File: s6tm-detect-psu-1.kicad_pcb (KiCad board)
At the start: 4 copper layers, 115 parts, among them J1 Conn_01x02, J2 Conn_01x02, J3 USB_C_Receptacle_USB2.0_14P, J4 Conn_01x04, J5 Conn_01x04, J6 Conn_01x04_Pin, J7 TC2030, SW1 SW_Push, SW2 SW_Push, U1 TPS259470x, U2 TPS259470x, U3 TPS259470x, U4 TPS62933, U5 TPS259470x, U6 SN65HVD230, U7 HT753-1, U8 STM32F103C8Tx, Y1 8M

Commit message: pcb: initial sectionning
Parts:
- moved D11 271.3 mm to (268.1, 71.2), turned to 90 degrees
- moved Y1 256.8 mm to (268.3, 61.2), turned to 90 degrees
- moved R27 254.0 mm to (271.9, 66.8), turned to 90 degrees
- moved D15 252.6 mm to (263.8, 34.9)
- moved C37 251.0 mm to (261.2, 39.2)
- moved SW1 250.8 mm to (247.0, 66.2)
- moved SW2 250.8 mm to (247.0, 70.8)
- moved C30 250.6 mm to (269.4, 66.8), turned to 90 degrees
- moved C29 247.2 mm to (266.9, 66.8), turned to 90 degrees
- moved J6 247.1 mm to (256.6, 71.1), turned to 90 degrees
- moved R28 246.0 mm to (272.6, 72.0), turned to 90 degrees
- moved U7 246.0 mm to (263.2, 92.3)
- moved R26 243.5 mm to (270.6, 72.0), turned to 90 degrees
- moved C27 240.9 mm to (272.4, 58.1), turned to 90 degrees
- moved C36 237.5 mm to (267.1, 74.9), turned to 90 degrees
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
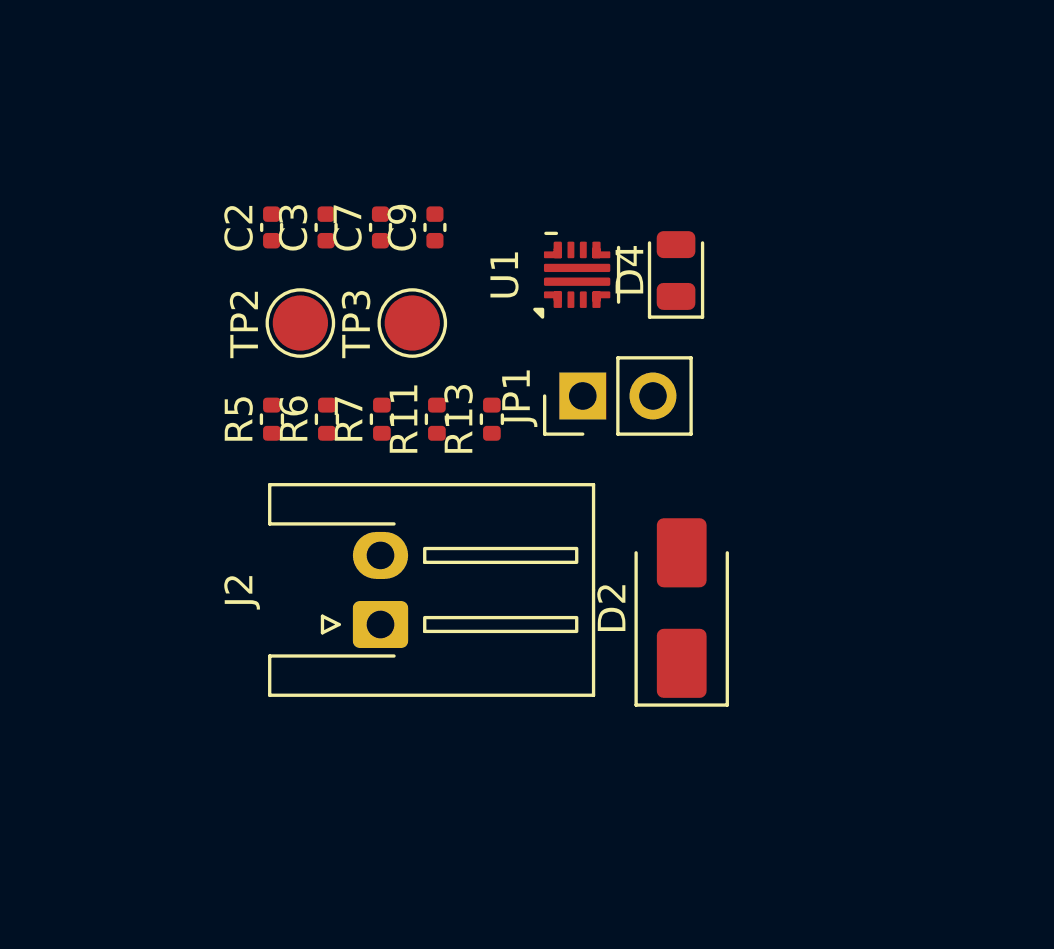
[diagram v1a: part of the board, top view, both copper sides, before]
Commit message: schem: update some 10u footprints
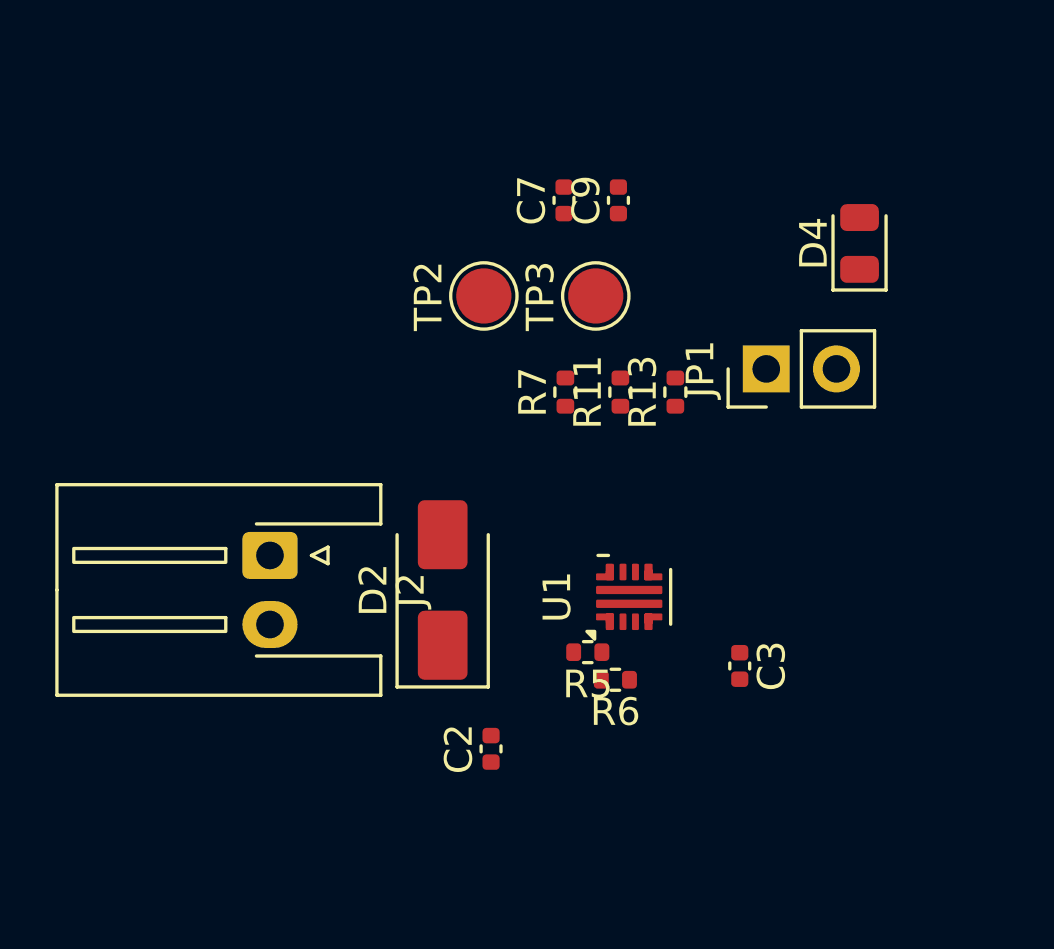
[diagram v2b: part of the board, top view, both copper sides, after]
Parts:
- moved C3 21.8 mm to (113.5, 61.0), turned to -90 degrees
- moved C2 20.5 mm to (104.5, 64.0)
- moved R5 14.2 mm to (108.0, 60.5), turned to 180 degrees
- moved R6 14.1 mm to (109.0, 61.5), turned to 180 degrees
- moved U1 11.8 mm to (109.5, 58.5)
- moved D2 8.67 mm to (102.8, 58.2)
- moved C7 6.71 mm to (107.1, 44.1)
- moved C9 6.71 mm to (109.1, 44.1)
- moved TP2 6.71 mm to (104.2, 47.6)
- moved TP3 6.71 mm to (108.3, 47.6)
- moved D4 6.71 mm to (117.8, 45.7)
- moved JP1 6.71 mm to (114.5, 50.2)
- moved R11 6.71 mm to (109.2, 51.1)
- moved R13 6.71 mm to (111.2, 51.1)
- moved R7 6.71 mm to (107.2, 51.1)
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
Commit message: pcb: add efuse 1 layout
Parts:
- C10, C7, C8, C9: footprint Capacitor_SMD:C_0402_1005Metric -> Capacitor_SMD:C_0805_2012Metric
- moved D4 17.0 mm to (110.5, 61.0), turned to 0 degrees
- moved C9 15.0 mm to (111.5, 59.0), turned to 0 degrees
- moved C7 12.6 mm to (110.8, 56.2)
- moved R13 12.3 mm to (107.3, 62.8), turned to 0 degrees
- moved R11 10.5 mm to (112.8, 61.0)
- moved C3 6.73 mm to (109.0, 56.0), turned to 90 degrees
- moved R7 5.42 mm to (107.5, 56.5), turned to 180 degrees
- moved C2 3.25 mm to (105.8, 61.0)
- moved R6 1.77 mm to (107.2, 61.8)
- moved U1 1.25 mm to (108.2, 58.5)
- moved R5 0.79 mm to (107.2, 60.8)

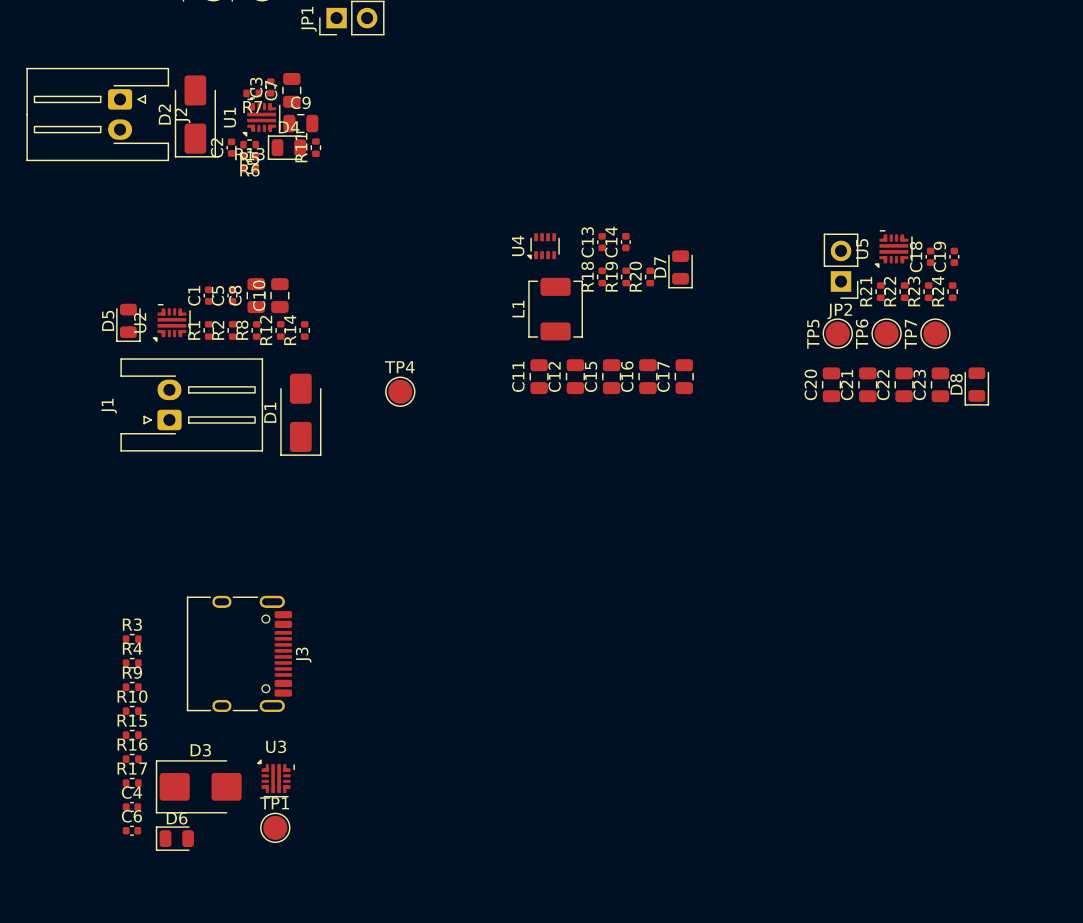
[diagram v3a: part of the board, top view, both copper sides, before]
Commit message: pcb: add efuse routing
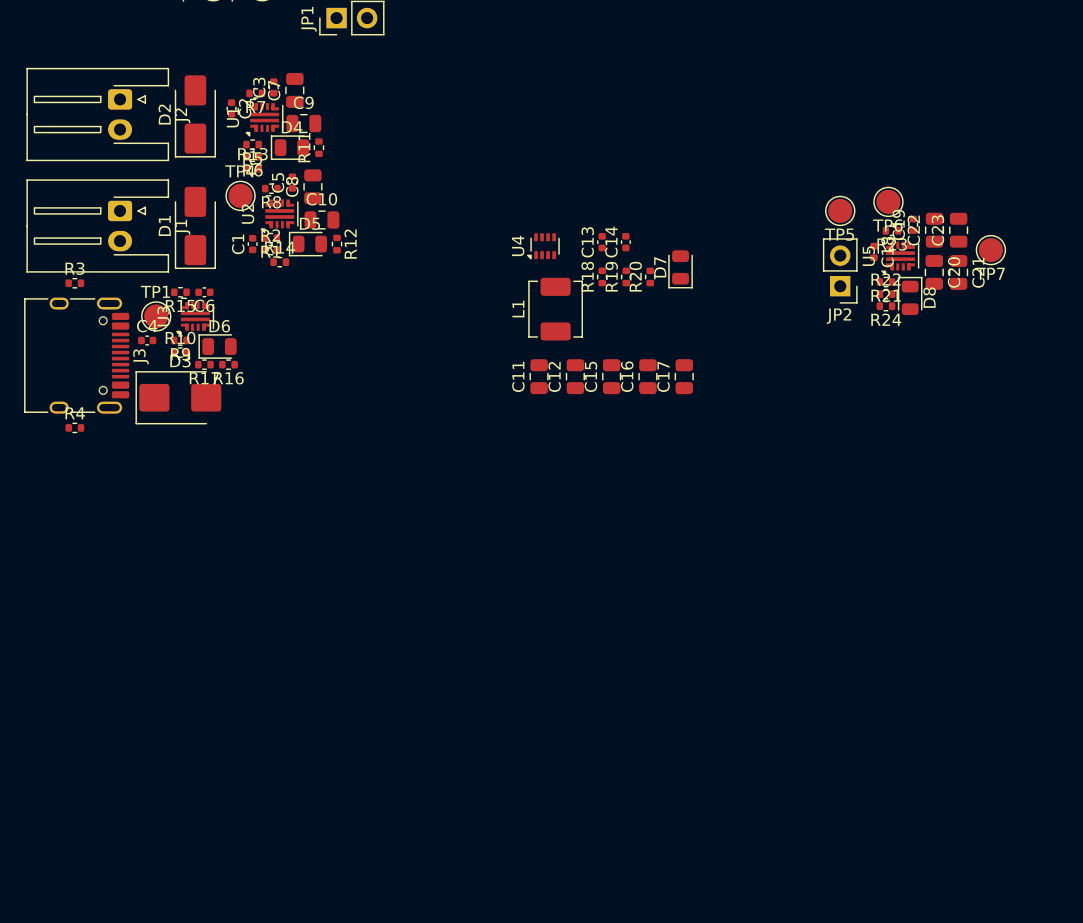
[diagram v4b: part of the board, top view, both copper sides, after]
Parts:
- moved C6 45.1 mm to (103.5, 73.0), turned to 180 degrees
- moved TP1 43.6 mm to (99.5, 75.0)
- moved D6 41.0 mm to (104.8, 77.5)
- moved U3 38.9 mm to (102.8, 75.0), turned to 90 degrees
- moved C4 38.7 mm to (98.8, 77.0)
- moved R15 37.0 mm to (101.5, 73.0), turned to 180 degrees
- moved R17 35.2 mm to (103.5, 79.0), turned to 180 degrees
- moved R16 33.7 mm to (105.5, 79.0), turned to 180 degrees
- moved D3 32.3 mm to (101.5, 81.8)
- moved R10 30.0 mm to (101.5, 78.0)
- moved R3 29.9 mm to (92.8, 72.2)
- moved R9 29.0 mm to (101.5, 77.0), turned to 180 degrees
- moved J3 28.2 mm to (92.5, 78.2)
- moved TP4 21.0 mm to (106.5, 65.0)
- moved R4 20.1 mm to (92.8, 84.2)
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
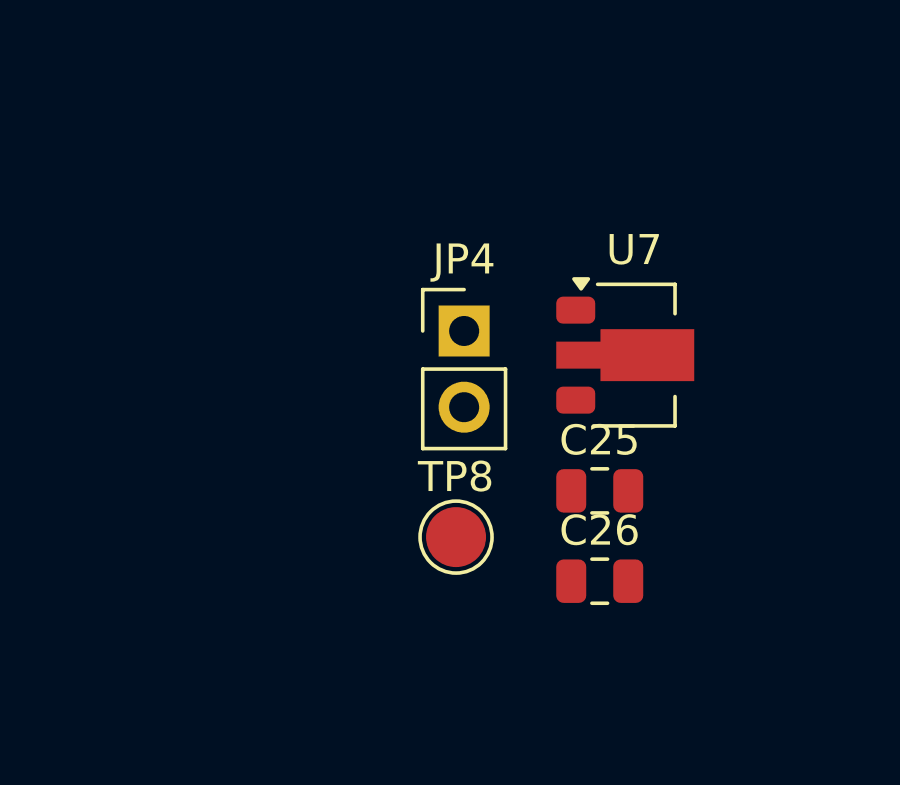
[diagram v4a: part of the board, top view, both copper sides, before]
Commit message: pcb: add ldo layout
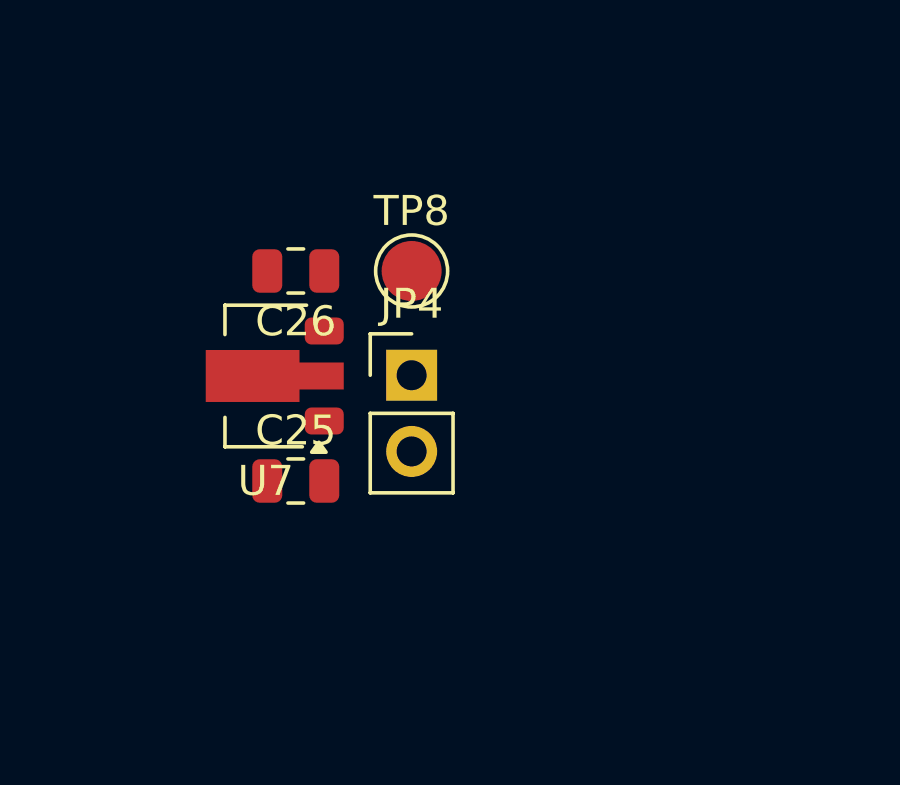
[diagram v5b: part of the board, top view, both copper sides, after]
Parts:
- moved C26 14.5 mm to (251.9, 89.5), turned to 180 degrees
- moved U7 12.3 mm to (250.9, 93.0), turned to 180 degrees
- moved C25 10.1 mm to (251.9, 96.5)
- moved TP8 8.99 mm to (255.8, 89.5)
- moved JP4 2.29 mm to (255.8, 93.0)
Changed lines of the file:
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@@
 	(footprint "TestPoint:TestPoint_Pad_D2.0mm"
 		(layer "F.Cu")
-		(at 257.23 98.37)
+		(at 255.75 89.5)
 		(descr "SMD pad as test Point, diameter 2.0mm")
 		(tags "test point SMD pad")
@@
 	(footprint "Capacitor_SMD:C_0805_2012Metric"
 		(layer "F.Cu")
-		(at 262.02 99.84)
+		(at 251.8875 89.5 180)
 		(descr "Capacitor SMD 0805 (2012 Metric), square (rectangular) end terminal, IPC-7351 nominal, (Body size source: IPC-SM-782 page 76, https://www.pcb-3d.com/wordpress/wp-content/uploads/ipc-sm-782a_amendment_1_and_2.pdf, https://docs.google.com/spreadsheets/d/1BsfQQcO9C6DZCsRaXUlFlo91Tg2WpOkGARC1WS5S8t0/edit?usp=sharing)")
 		(tags "capacitor")
@@
 		)
 		(property "Basic" "Y"
-			(at 0 0 0)
+			(at 0 0 180)
 			(unlocked yes)
 			(layer "F.Fab")
@@
 		)
 		(property "JLCPCB Part #" "C440198"
-			(at 0 0 0)
+			(at 0 0 180)
 			(unlocked yes)
 			(layer "F.Fab")
@@
 		)
 		(property "Manufacturer" "Murata"
-			(at 0 0 0)
+			(at 0 0 180)
 			(unlocked yes)
 			(layer "F.Fab")
@@
 		)
 		(property "Manufacturer Part Number" "GRM21BR61H106KE43L"
-			(at 0 0 0)
+			(at 0 0 180)
 			(unlocked yes)
 			(layer "F.Fab")
@@
 		(duplicate_pad_numbers_are_jumpers no)
 		(fp_line
-			(start -0.261252 -0.735)
-			(end 0.261252 -0.735)
+			(start -0.261252 0.735)
+			(end 0.261252 0.735)
 			(stroke
 				(width 0.12)
@@
 		)
 		(fp_line
-			(start -0.261252 0.735)
-			(end 0.261252 0.735)
+			(start -0.261252 -0.735)
+			(end 0.261252 -0.735)
 			(stroke
 				(width 0.12)
@@
 		)
 		(pad "1" smd roundrect
-			(at -0.95 0)
+			(at -0.95 0 180)
 			(size 1 1.45)
 			(layers "F.Cu" "F.Mask" "F.Paste")
@@
 		)
 		(pad "2" smd roundrect
-			(at 0.95 0)
+			(at 0.95 0 180)
 			(size 1 1.45)
 			(layers "F.Cu" "F.Mask" "F.Paste")
@@
 	(footprint "Capacitor_SMD:C_0805_2012Metric"
 		(layer "F.Cu")
-		(at 262.02 96.83)
+		(at 251.8875 96.5)
 		(descr "Capacitor SMD 0805 (2012 Metric), square (rectangular) end terminal, IPC-7351 nominal, (Body size source: IPC-SM-782 page 76, https://www.pcb-3d.com/wordpress/wp-content/uploads/ipc-sm-782a_amendment_1_and_2.pdf, https://docs.google.com/spreadsheets/d/1BsfQQcO9C6DZCsRaXUlFlo91Tg2WpOkGARC1WS5S8t0/edit?usp=sharing)")
 		(tags "capacitor")
@@
 	(footprint "Connector_PinHeader_2.54mm:PinHeader_1x02_P2.54mm_Vertical"
 		(layer "F.Cu")
-		(at 257.5 91.5)
+		(at 255.75 92.975)
 		(descr "Through hole straight pin header, 1x02, 2.54mm pitch, single row")
 		(tags "Through hole pin header THT 1x02 2.54mm single row")
@@
 	(footprint "Package_TO_SOT_SMD:SOT-89-3"
 		(layer "F.Cu")
-		(at 263.17 92.305)
+		(at 250.8875 93 180)
 		(descr "SOT-89-3, http://ww1.microchip.com/downloads/en/DeviceDoc/3L_SOT-89_MB_C04-029C.pdf")
 		(tags "SOT-89-3")
@@
 		)
 		(property "Datasheet" "https://www.holtek.com/documents/10179/116711/HT75xx-1v250.pdf"
-			(at 0 0 0)
+			(at 0 0 180)
 			(unlocked yes)
 			(layer "F.Fab")
@@
 		)
 		(property "Description" "100mA Low Dropout Voltage Regulator, Fixed Output, SOT89"
-			(at 0 0 0)
+			(at 0 0 180)
 			(unlocked yes)
 			(layer "F.Fab")
@@
 		)
 		(property "Basic" "Y"
-			(at 0 0 0)
+			(at 0 0 180)
 			(unlocked yes)
 			(layer "F.Fab")
@@
 		)
 		(property "JLCPCB Part #" "C14289"
-			(at 0 0 0)
+			(at 0 0 180)
 			(unlocked yes)
 			(layer "F.Fab")
@@
 		)
 		(property "Manufacturer" "Holtek Semicon"
-			(at 0 0 0)
+			(at 0 0 180)
 			(unlocked yes)
 			(layer "F.Fab")
@@
 		)
 		(property "Manufacturer Part Number" "HT7533-1"
-			(at 0 0 0)
+			(at 0 0 180)
 			(unlocked yes)
 			(layer "F.Fab")
@@
 		(duplicate_pad_numbers_are_jumpers no)
 		(fp_line
-			(start -1.22 -2.36)
-			(end 1.36 -2.36)
+			(start 1.36 2.36)
+			(end -1.36 2.36)
 			(stroke
 				(width 0.12)
@@
 		)
 		(fp_line
-			(start 1.36 -1.38)
-			(end 1.36 -2.36)
+			(start 1.36 1.38)
+			(end 1.36 2.36)
 			(stroke
 				(width 0.12)
@@
 		)
 		(fp_line
-			(start 1.36 1.38)
-			(end 1.36 2.36)
+			(start 1.36 -1.38)
+			(end 1.36 -2.36)
 			(stroke
 				(width 0.12)
@@
 		)
 		(fp_line
-			(start 1.36 2.36)
-			(end -1.36 2.36)
+			(start -1.22 -2.36)
+			(end 1.36 -2.36)
 			(stroke
 				(width 0.12)
@@
 		)
 		(fp_line
-			(start -2.85 2.5)
-			(end -2.85 -2.5)
+			(start 2.25 -2.5)
+			(end 2.25 2.5)
 			(stroke
 				(width 0.05)
@@
 		)
 		(fp_line
-			(start -2.85 2.5)
-			(end 2.25 2.5)
+			(start 2.25 -2.5)
+			(end -2.85 -2.5)
 			(stroke
 				(width 0.05)
@@
 		)
 		(fp_line
-			(start 2.25 -2.5)
-			(end -2.85 -2.5)
+			(start -2.85 2.5)
+			(end 2.25 2.5)
 			(stroke
 				(width 0.05)
@@
 		)
 		(fp_line
-			(start 2.25 -2.5)
-			(end 2.25 2.5)
+			(start -2.85 2.5)
+			(end -2.85 -2.5)
 			(stroke
 				(width 0.05)
@@
 		)
 		(fp_line
-			(start -1.25 -1.25)
-			(end -0.25 -2.25)
+			(start 1.25 2.25)
+			(end -1.25 2.25)
 			(stroke
 				(width 0.1)
@@
 		)
 		(fp_line
-			(start -1.25 2.25)
-			(end -1.25 -1.25)
+			(start 1.25 -2.25)
+			(end 1.25 2.25)
 			(stroke
 				(width 0.1)
@@
 		)
 		(fp_line
-			(start 1.25 -2.25)
-			(end 1.25 2.25)
+			(start -1.25 2.25)
+			(end -1.25 -1.25)
 			(stroke
 				(width 0.1)
@@
 		)
 		(fp_line
-			(start 1.25 2.25)
-			(end -1.25 2.25)
+			(start -1.25 -1.25)
+			(end -0.25 -2.25)
 			(stroke
 				(width 0.1)
@@
 		)
 		(pad "1" smd roundrect
-			(at -1.95 -1.5)
+			(at -1.95 -1.5 180)
 			(size 1.3 0.9)
 			(layers "F.Cu" "F.Mask" "F.Paste")
@@
 		)
 		(pad "2" smd custom
-			(at -1.8625 0)
+			(at -1.8625 0 180)
 			(size 1.475 0.9)
 			(layers "F.Cu" "F.Mask" "F.Paste")
@@
 		)
 		(pad "3" smd roundrect
-			(at -1.95 1.5)
+			(at -1.95 1.5 180)
 			(size 1.3 0.9)
 			(layers "F.Cu" "F.Mask" "F.Paste")
